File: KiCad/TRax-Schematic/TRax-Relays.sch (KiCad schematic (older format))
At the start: 15 parts, among them J10 Parked, J11 Fob, J12 Inputs, J13 Relays, J14 Inputs, J15 Relays, J4 WX, J7 RoofPower, J8 MountPower, J9 Open/Close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

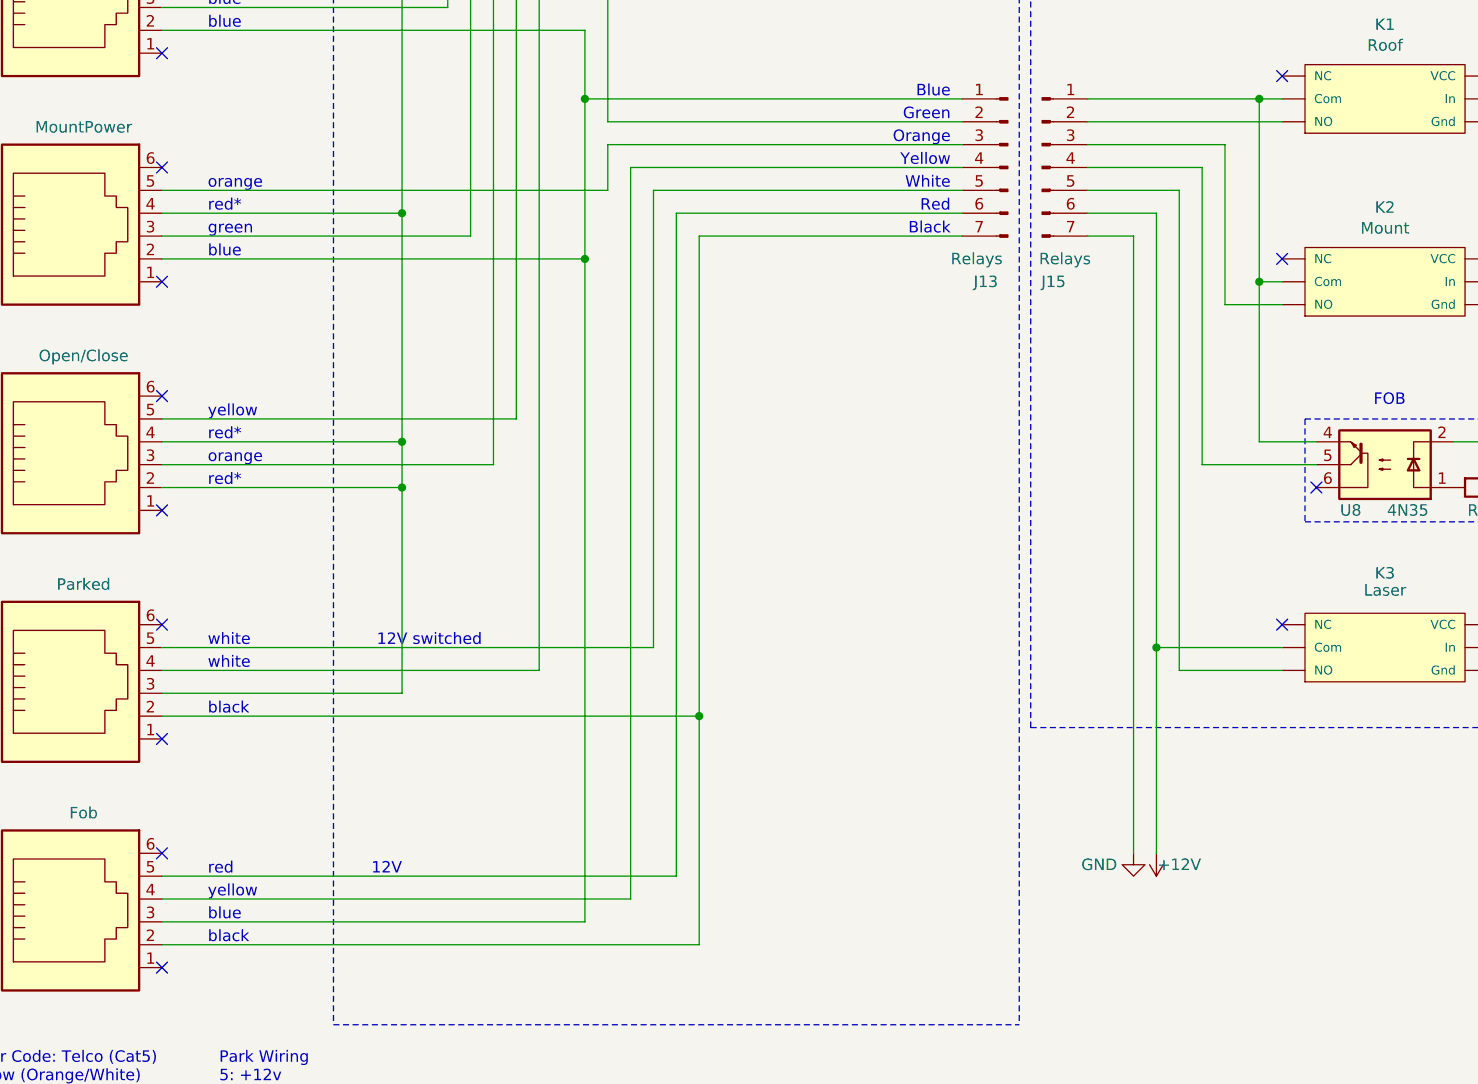
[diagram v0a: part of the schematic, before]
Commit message: updated schematic (v1.7) direct wire fob isolator to fob tigger
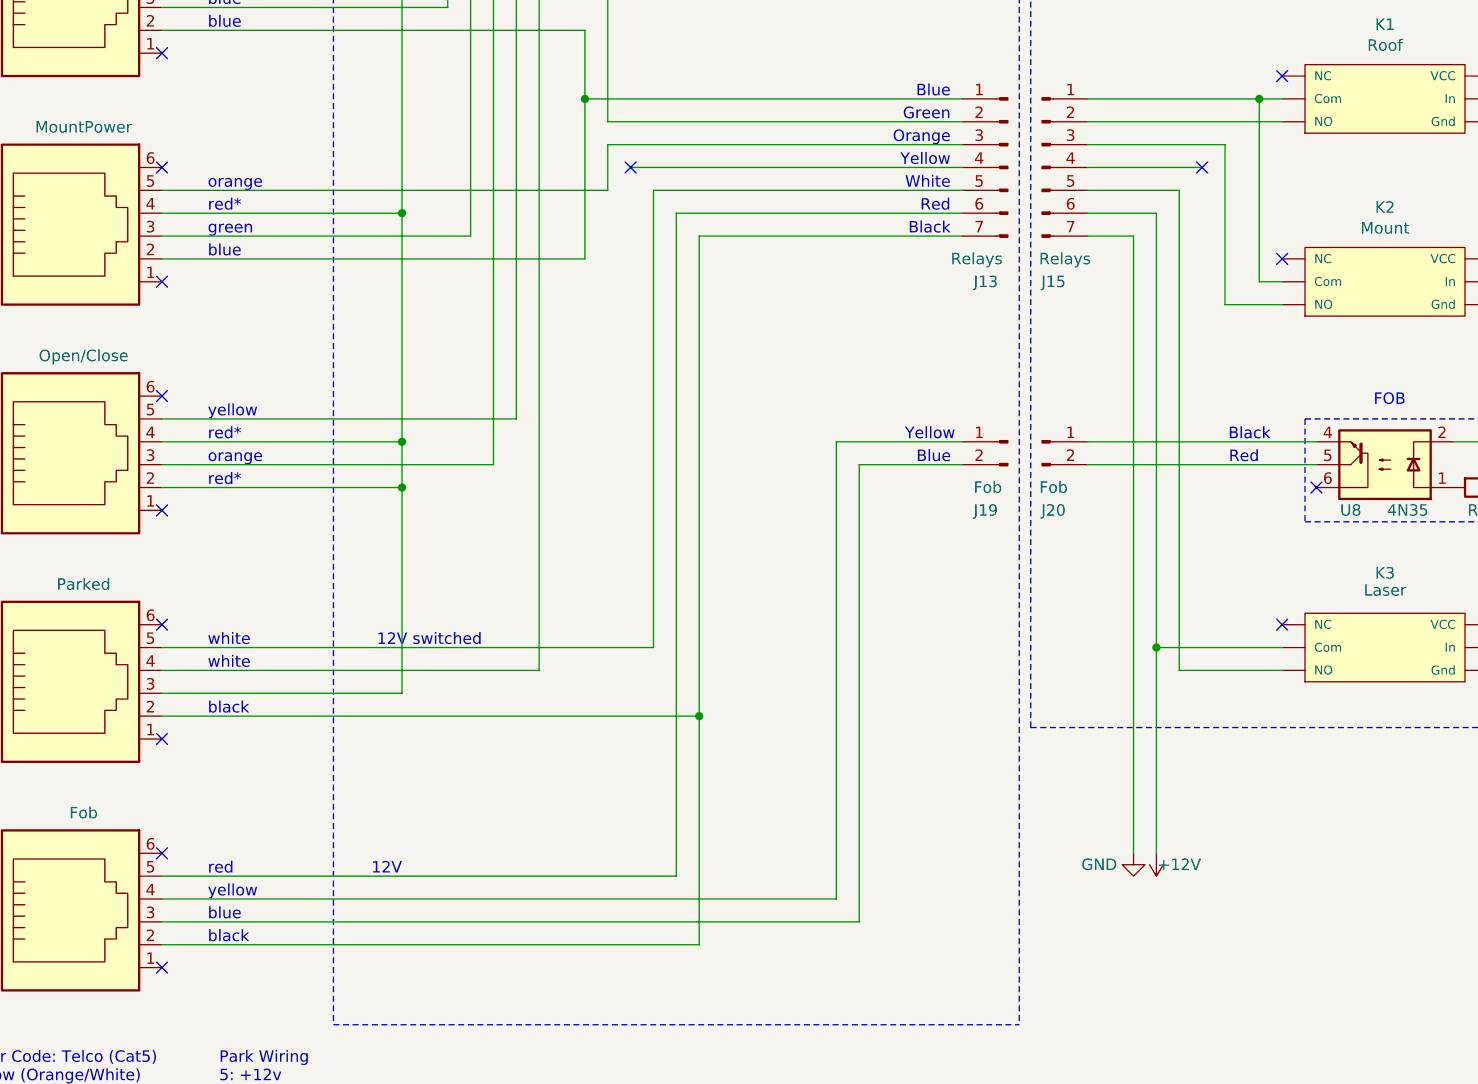
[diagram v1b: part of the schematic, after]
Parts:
- added J19, J20: Fob, symbol Connector:Conn_01x02_Male
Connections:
- net at J13.1 (Pin_1), J7.2, J8.2: no longer J11.3
- net at J11.4: now also J19.1 (Pin_1); no longer J13.4 (Pin_4)
- net at J15.4 (Pin_4): no longer U8.5
- net at K1.~ (VCC): now also K2.~ (VCC), K3.~ (VCC)
- new net: J11.3, J19.2 (Pin_2)
- new net: J15.1 (Pin_1), K1.~ (VCC), K2.~ (VCC)
- new net: K1.~ (VCC), K2.~ (VCC), K3.~ (VCC), U8.2
- new net: J20.1 (Pin_1), U8.4
- new net: J20.2 (Pin_2), U8.5
- now unconnected: K2.~ (VCC), K2.~ (VCC), K2.~ (VCC)
- no-connect marks 18 -> 20
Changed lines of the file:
@@
 Sheet 2 3
 Title "T-Rax Relays & Connector wiring"
-Date "2021-10-17"
-Rev "v1.6"
+Date "2021-10-31"
+Rev "v1.7"
 Comp "Robert Ferguson Observatory"
 Comment1 "David Kensiski"
-Comment2 "v1.4 add park sensor isolator (never implemented)"
-Comment3 "v1.5 remove park isolator (see detector module); replace fob relay with isolator"
-Comment4 "v1.6 merge all schematics into one doc; add accessory modules"
+Comment2 "v1.5 remove park isolator (see detector module); replace fob relay with isolator"
+Comment3 "v1.6 merge all schematics into one doc; add accessory modules"
+Comment4 "v1.7 direct wire fob isolator to fob trigger "
 $EndDescr
 Text Notes 5450 1050 2    50   ~ 0
@@
 Wire Wire Line
 	6800 3000 6900 3000
-Connection ~ 6800 3800
-Wire Wire Line
-	6800 3800 6800 4500
-Wire Wire Line
-	2000 6500 4050 6500
 $Comp
 L Connector:Conn_01x07_Male J15
@@
 Wire Wire Line
 	3950 3200 3950 3400
-Wire Wire Line
-	4050 3300 4050 6500
-Wire Wire Line
-	3850 6600 3850 3700
-Connection ~ 3850 3700
-Wire Wire Line
-	2000 6600 3850 6600
 Wire Wire Line
 	2000 3700 3850 3700
@@
 Wire Wire Line
 	8200 4500 8200 5500
-Wire Wire Line
-	6550 3300 6550 4600
 NoConn ~ 7050 4700
 $Comp
@@
 Wire Wire Line
 	8200 4500 7650 4500
-Wire Wire Line
-	6550 4600 7050 4600
-Wire Wire Line
-	6800 4500 7050 4500
 Wire Notes Line
 	7000 4850 7950 4850
@@
 Wire Wire Line
 	2000 5600 3050 5600
+$Comp
+L Connector:Conn_01x02_Male J19
+U 1 1 6180CA74
+P 5700 4500
+F 0 "J19" H 5850 4200 50  0000 R CNN
+F 1 "Fob" H 5850 4300 50  0000 R CNN
+F 2 "" H 5700 4500 50  0001 C CNN
+F 3 "~" H 5700 4500 50  0001 C CNN
+	1    5700 4500
+	-1   0    0    -1
+$EndComp
+$Comp
+L Connector:Conn_01x02_Male J20
+U 1 1 6180D475
+P 5850 4500
+F 0 "J20" H 5900 4200 50  0000 C CNN
+F 1 "Fob" H 5900 4300 50  0000 C CNN
+F 2 "" H 5850 4500 50  0001 C CNN
+F 3 "~" H 5850 4500 50  0001 C CNN
+	1    5850 4500
+	1    0    0    -1
+$EndComp
+Wire Wire Line
+	6050 4500 7050 4500
+Wire Wire Line
+	6050 4600 7050 4600
+NoConn ~ 6550 3300
+Wire Wire Line
+	4950 6500 4950 4500
+Wire Wire Line
+	4950 4500 5500 4500
+Wire Wire Line
+	5050 6600 5050 4600
+Wire Wire Line
+	5050 4600 5500 4600
+Wire Wire Line
+	2000 6600 5050 6600
+Wire Wire Line
+	2000 6500 4950 6500
+NoConn ~ 4050 3300
+Text Notes 6800 4600 2    50   ~ 0
+Red
+Text Notes 6850 4500 2    50   ~ 0
+Black
 Wire Bus Line
 	8900 2450 10500 2450
 Wire Bus Line
 	6200 1150 6200 1850
+Text Notes 5250 4500 0    50   ~ 0
+Yellow
+Text Notes 5300 4600 0    50   ~ 0
+Blue
 $EndSCHEMATC
